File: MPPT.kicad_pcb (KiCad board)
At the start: 2 copper layers, 172.7 x 116.8 mm, 155 parts, among them J1 Solar Array, J2 Battery, J3 Car Power, J4 CAN_In, J5 CAN_Out, Q1 NMOS, Q2 NMOS, SW1 RESET, SW2 CAN Address, U1 PQMC3-D12-S9-S, U2 Nucleo_L432KC, U3 UCC37321, U4 INA210, U5 ADM3055E, U6 INA210, U7 CDSOT23-T24CAN

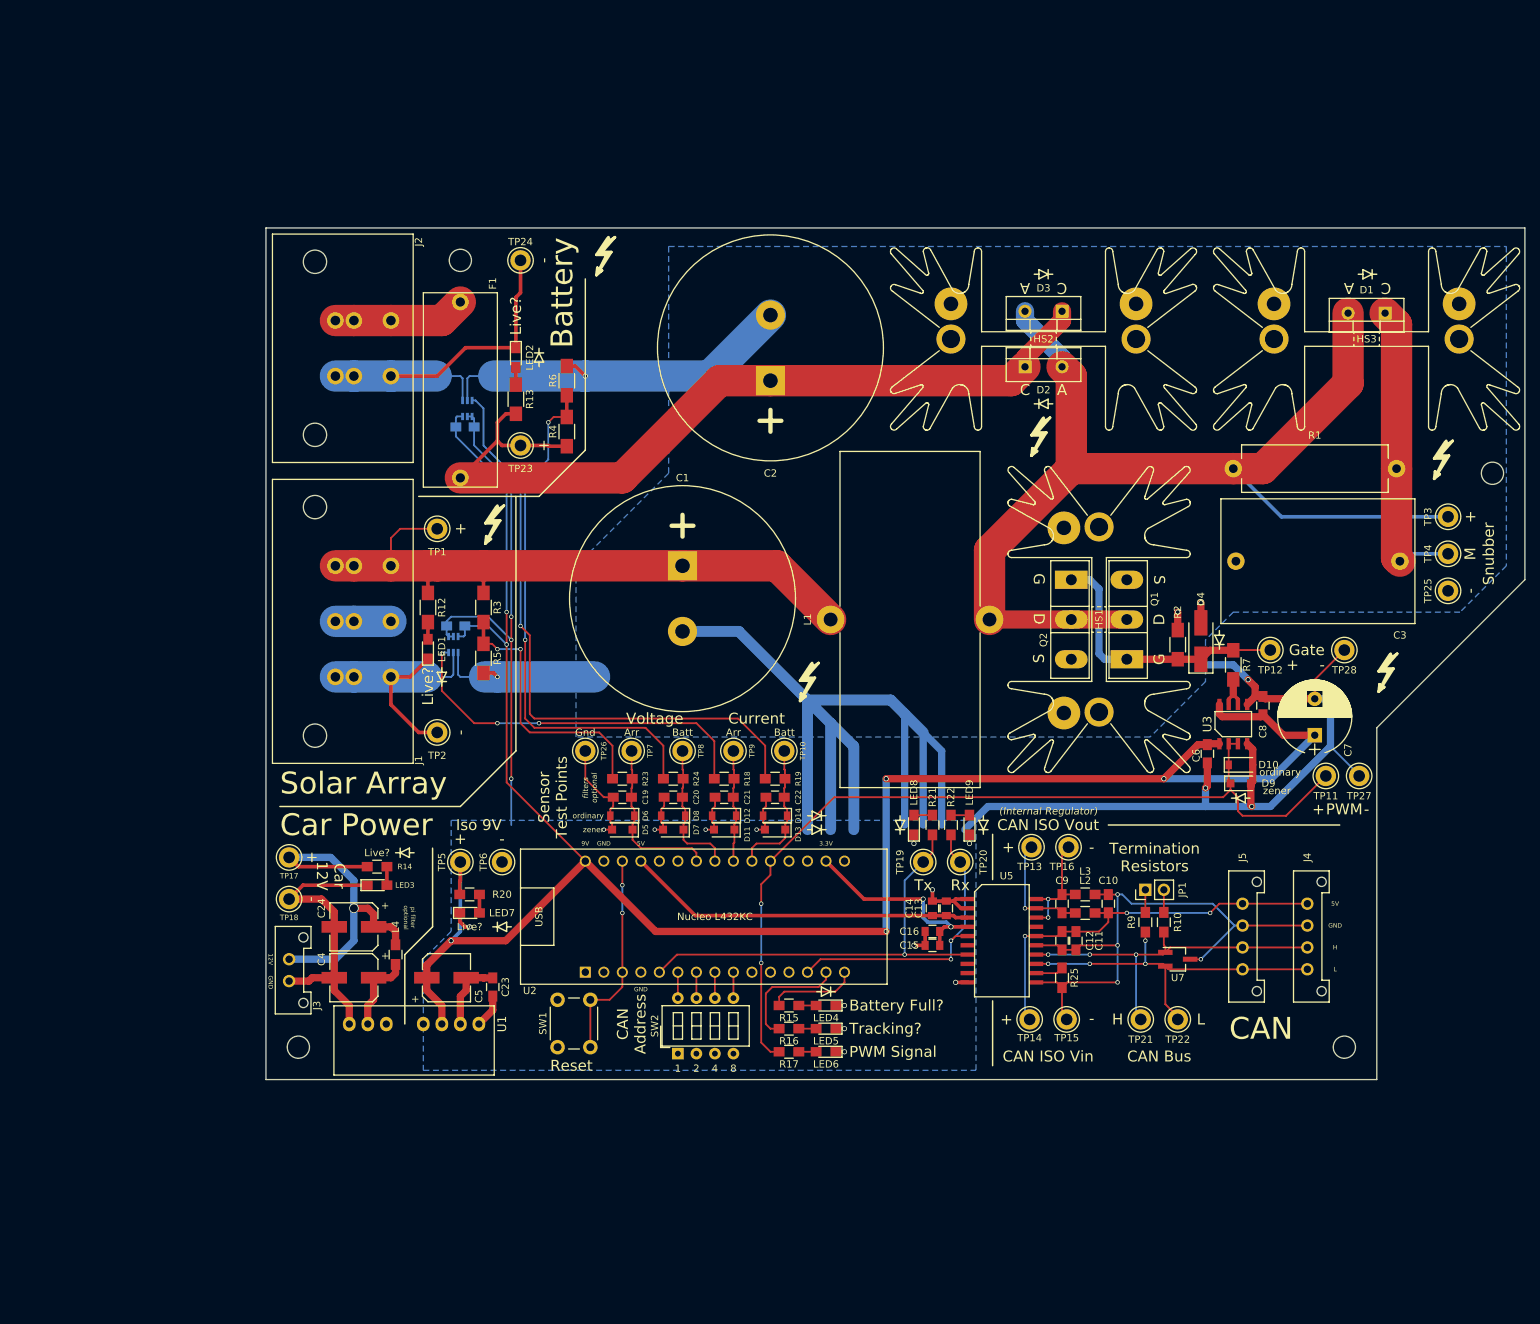
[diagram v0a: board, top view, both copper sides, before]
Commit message: added unity gain op amp buffer to voltage sensors
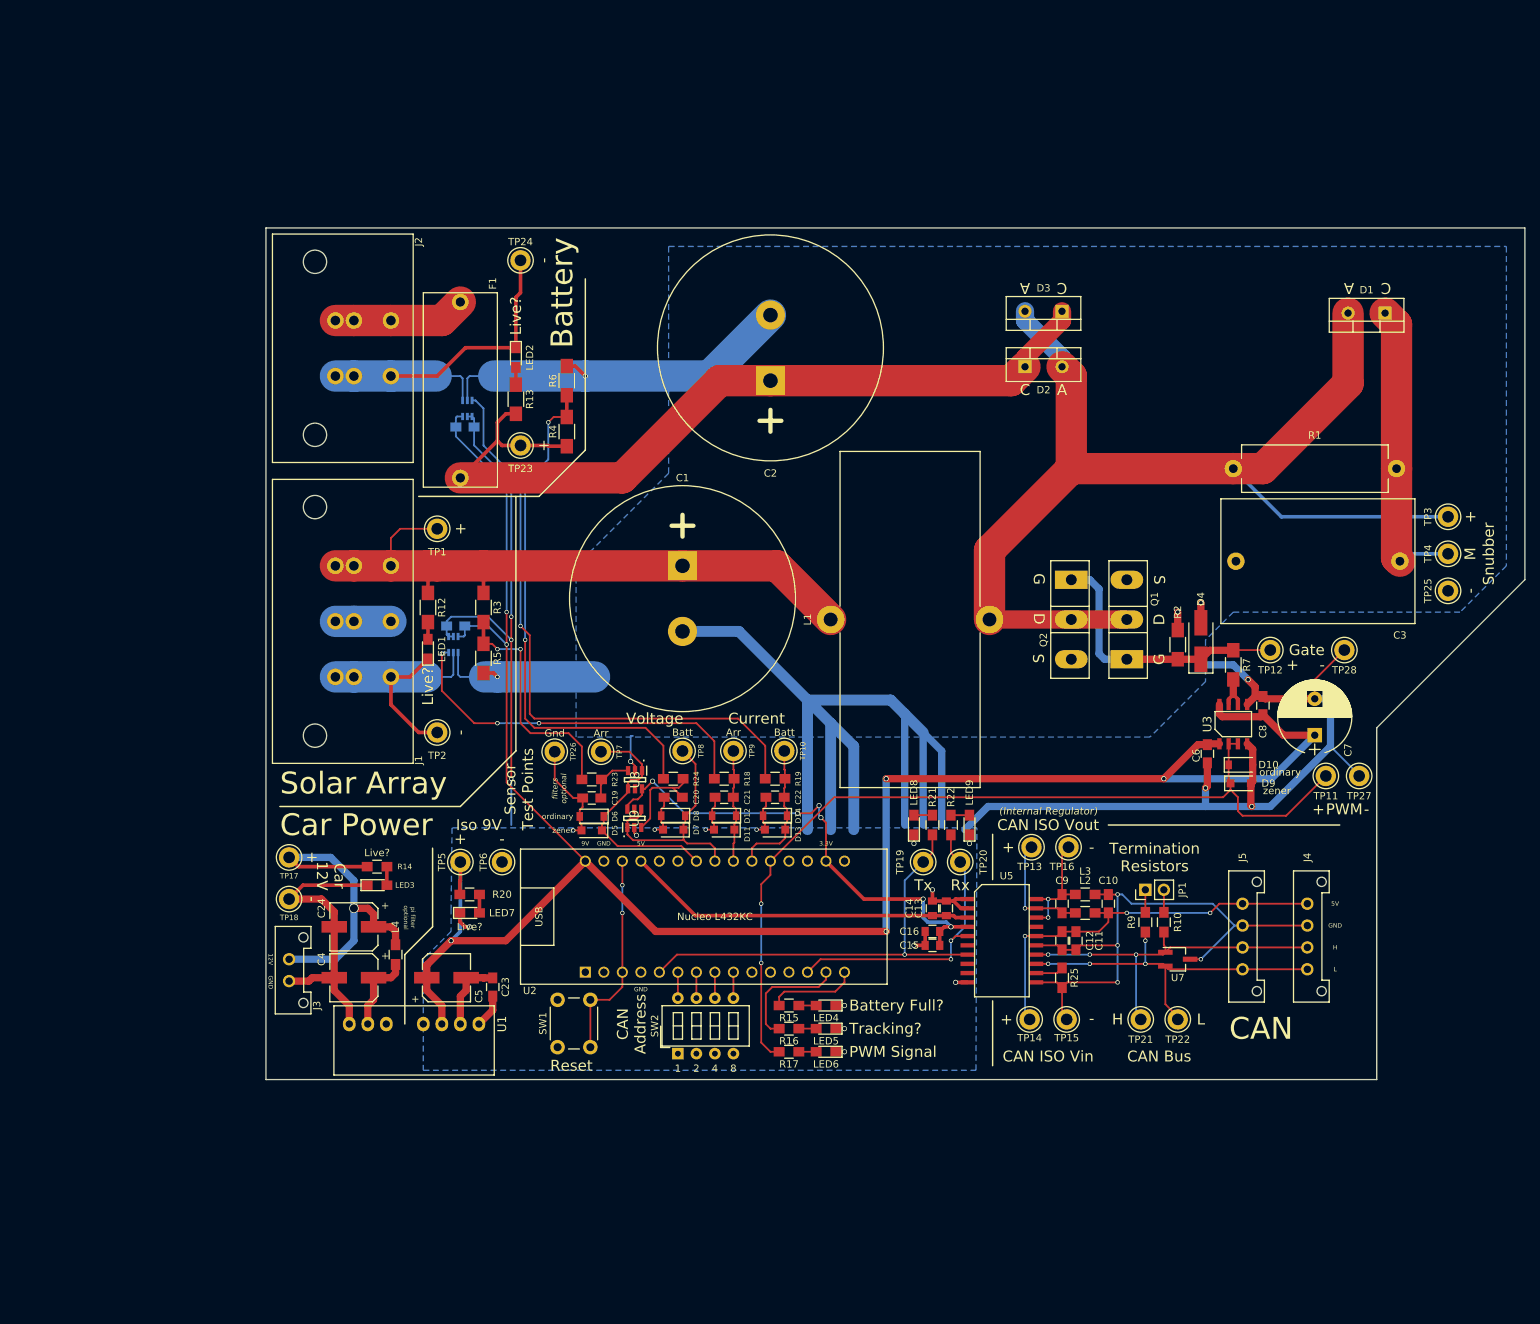
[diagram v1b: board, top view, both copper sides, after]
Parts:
- removed HS1, HS2, HS3: Heatsink_Fischer_SK129-STS_42x25mm_2xDrill2.5mm, Heatsinks:Heatsink_Fischer_SK129-STS_42x25mm_2xDrill2.5mm
- removed REF** (x6): Symbol_HighVoltage_Small, UTSVT_Special:Symbol_HighVoltage_Small
- removed REF** (x6): SolderWirePad_single_2mmDrill, Wire_Pads:SolderWirePad_single_2mmDrill
- removed REF** (x4): MountingHole_4-40_PanHead, UTSVT_Mechanical:MountingHole_4-40_PanHead
- removed REF** (x14): Diode_Symbol_Small, UTSVT_Special:Diode_Symbol_Small
- added U8: MAX400_option2, MPPT_Custom:SOT95P280X145-6N, F.Cu at (81.8, 106.8)
- added U9: MAX400_option2, MPPT_Custom:SOT95P280X145-6N, F.Cu at (81.7, 112.1)
- moved C19 4.20 mm to (75.8, 109.3)
- moved D5 4.20 mm to (75.8, 113.8)
- moved D6 4.20 mm to (75.8, 111.9)
- moved R23 4.20 mm to (75.8, 106.8)
- moved TP26 4.20 mm to (70.7, 103.0)
- moved TP7 4.20 mm to (77.1, 103.0)
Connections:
- C19 pad 1: /Array_Voltage -> Net-(C19-Pad1)
- C20 pad 1: /Battery_Voltage -> Net-(C20-Pad1)
- R23 pad 2: /Array_Voltage -> Net-(C19-Pad1)
- R24 pad 2: /Battery_Voltage -> Net-(C20-Pad1)
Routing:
- net +3V3: track 28.4 -> 67.4 mm, vias 2 -> 6
- net /Battery_Voltage: track 19.1 -> 33.0 mm
- net Net-(C20-Pad1): track 0.00 -> 12.8 mm
- net /Array_Voltage: track 23.2 -> 33.0 mm
- net GNDPWR: track 463.5 -> 470.0 mm, vias 23 -> 25
- net Net-(C19-Pad1): track 0.00 -> 6.01 mm
- net Net-(R23-Pad1): track 37.0 -> 32.8 mm
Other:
- board text added: "."

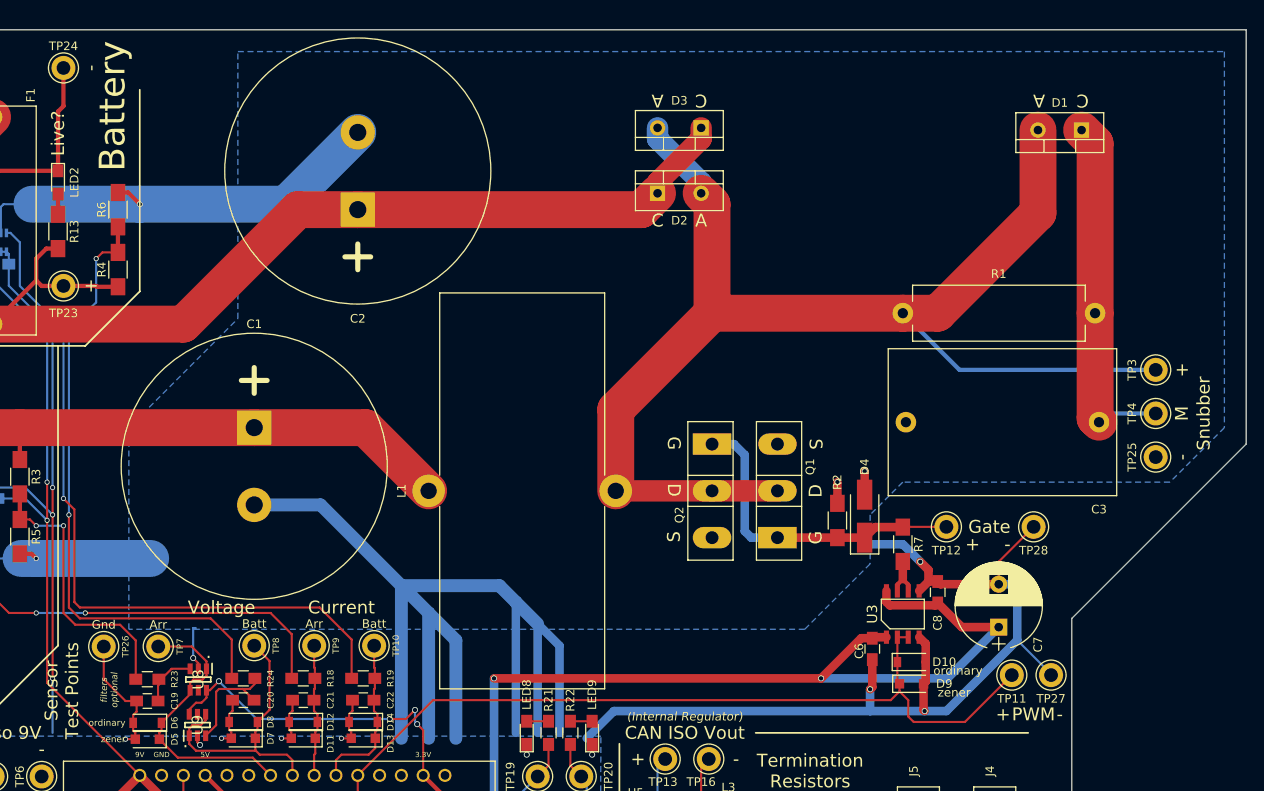
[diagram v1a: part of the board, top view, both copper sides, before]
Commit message: added back in heatsinks and generated gerber.
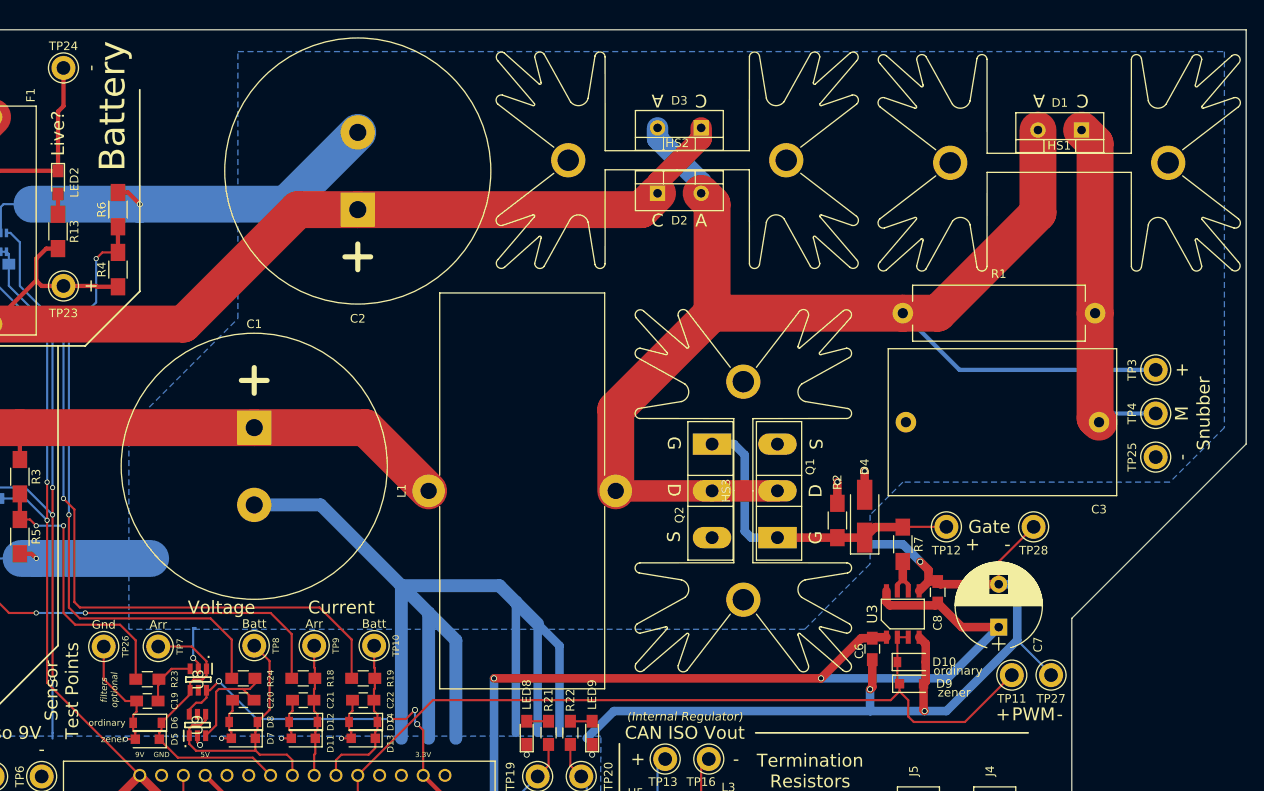
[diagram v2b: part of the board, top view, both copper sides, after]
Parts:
- added HS1: Heatsink, Heatsink:Heatsink_Fischer_SK129-STS_42x25mm_2xDrill2.5mm, F.Cu at (182.1, 46.6)
- added HS2: Heatsink, Heatsink:Heatsink_Fischer_SK129-STS_42x25mm_2xDrill2.5mm, F.Cu at (137.6, 46.3)
- added HS3: Heatsink, Heatsink:Heatsink_Fischer_SK129-STS_42x25mm_2xDrill2.5mm, F.Cu at (145.2, 84.8)
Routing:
- net GNDPWR: track 470.0 -> 470.7 mm
